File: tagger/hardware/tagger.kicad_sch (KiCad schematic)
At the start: 27 parts, among them J4 SWD, J7 TETHER_DATA, J8 DISPLAY, J9 IO_CONN, Q1 Q_NMOS_GSD, SW24 BOOT0, SW26 NRST, U2 STM32F103RGTx, Y3 CG04874-8M

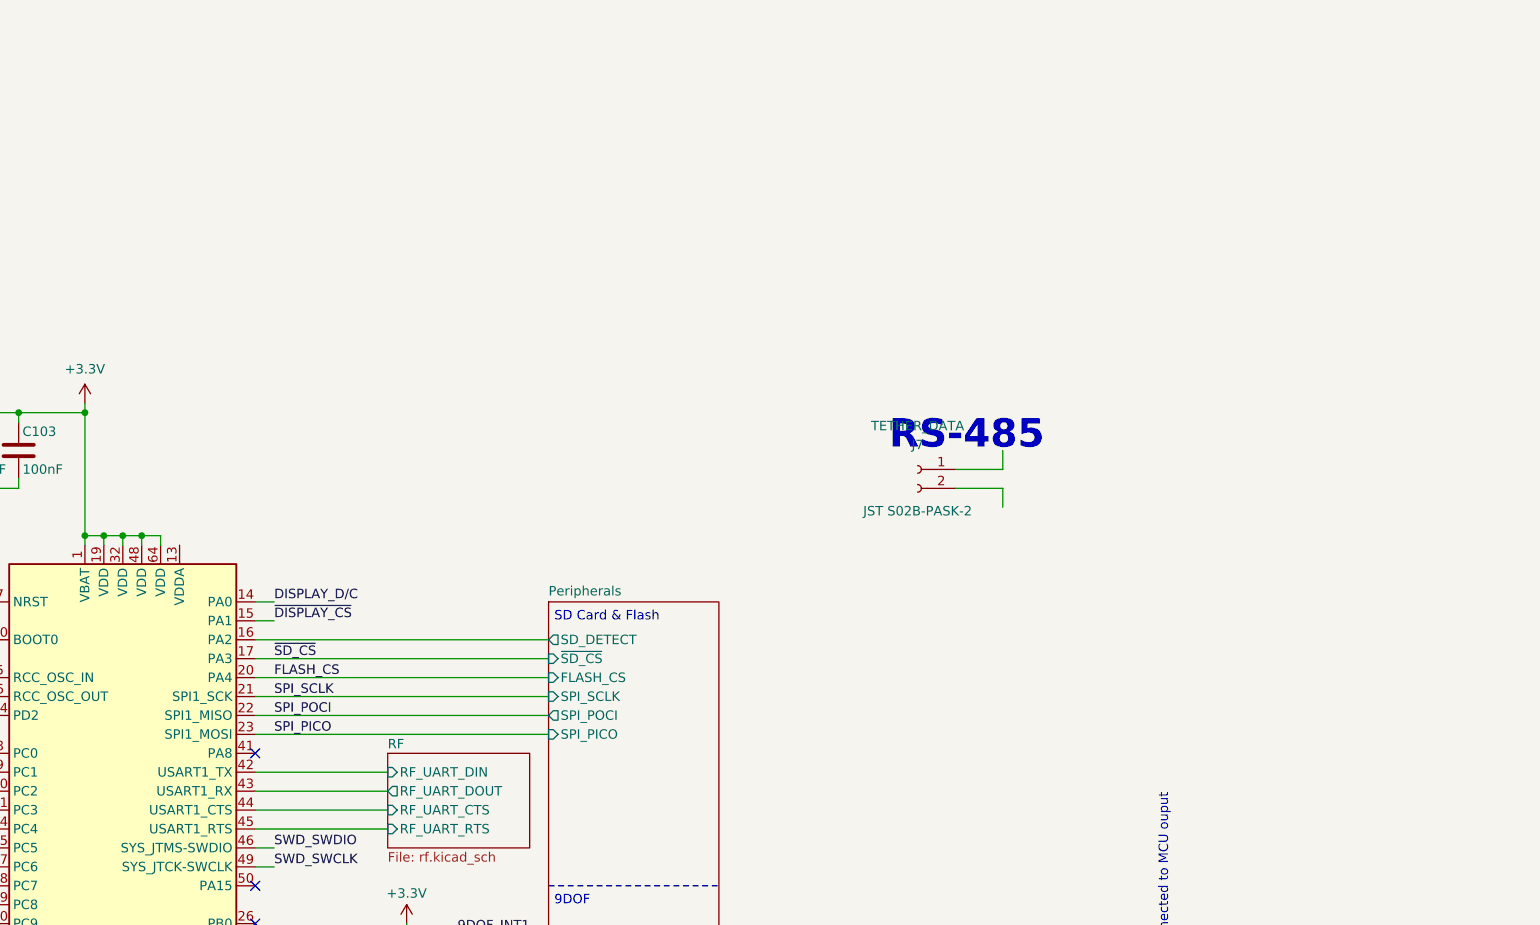
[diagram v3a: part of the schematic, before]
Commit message: feat: board routing and RS485 implementation
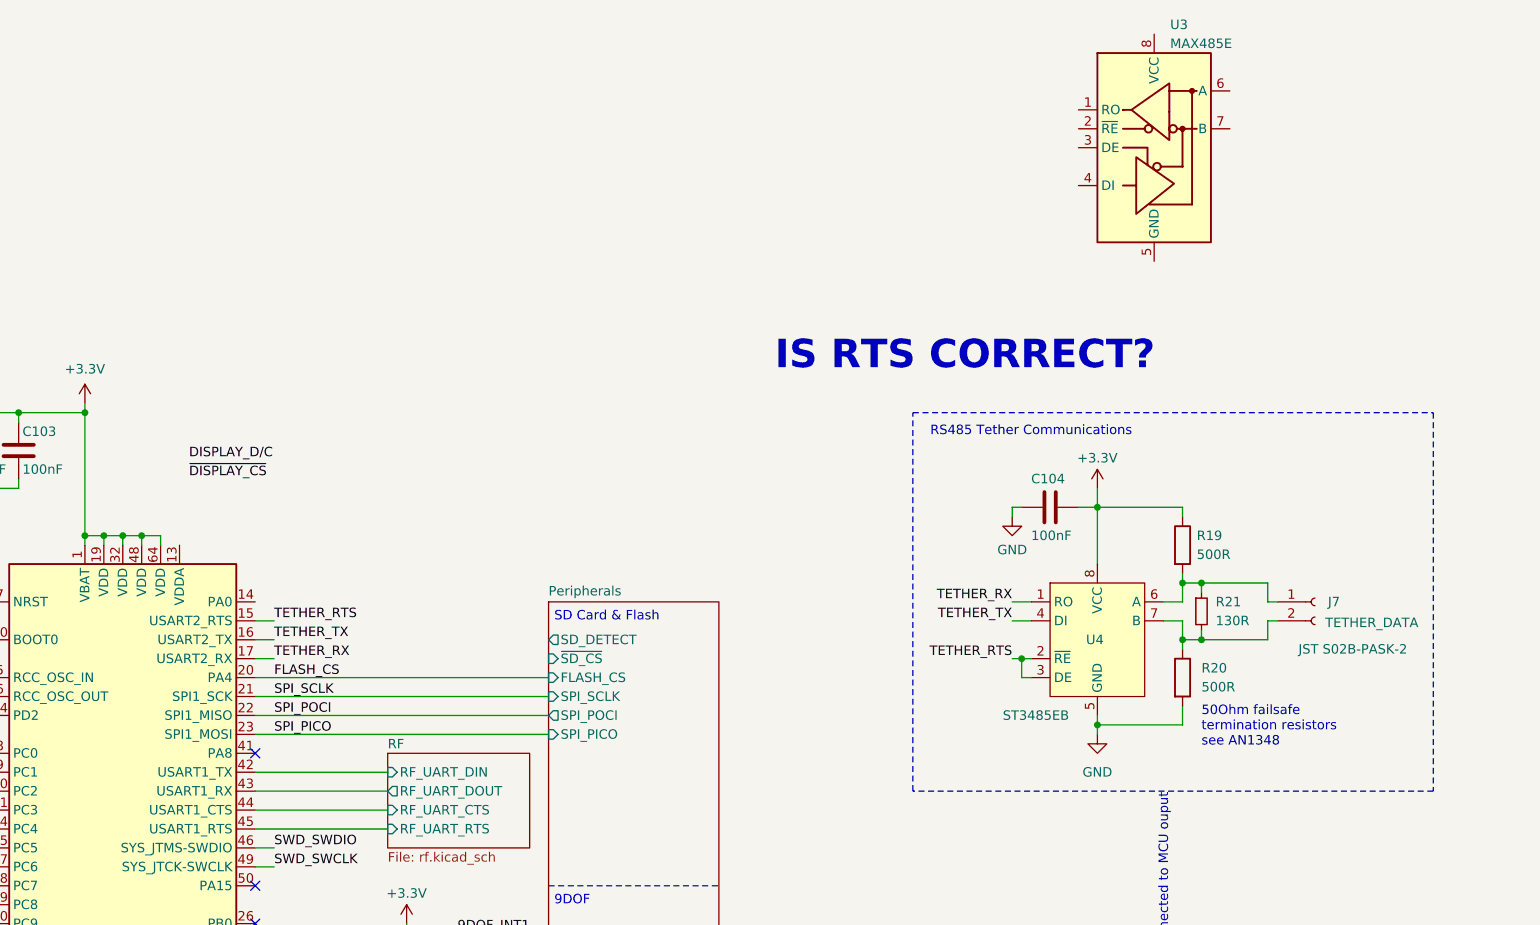
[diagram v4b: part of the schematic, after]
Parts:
- added C104: 100nF, Capacitor_SMD:C_0201_0603Metric_Pad0.64x0.40mm_HandSolder, symbol Device:C
- added R19, R20: 500R, symbol Device:R
- added R21: 130R, symbol Device:R_Small
- added U3: MAX485E, Package_SO:SOIC-8_3.9x4.9mm_P1.27mm, symbol Interface_UART:MAX485E
- added U4: ST3485EB, Package_SO:SOIC-8-N7_3.9x4.9mm_P1.27mm, symbol ST3485EBDR:ST3485EBDR
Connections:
- net +3.3V: now also C104.1, R19.1, U4.8 (VCC)
- net DISPLAY_D/C: no longer U2.14 (PA0)
- net GND: now also C104.2, R20.2, U4.5 (GND)
- net Peripherals/SD_DETECT: no longer U2.16 (PA2)
- net ~{DISPLAY_CS}: no longer U2.15 (PA1)
- net at J7.1 (Pin_1): now also R19.2, R21.1, U4.6 (A)
- net at J7.2 (Pin_2): now also R20.1, R21.2, U4.7 (B)
- net ~{SD_CS} renamed TETHER_RX
- net TETHER_RX: now also U4.1 (RO)
- new net TETHER_RTS: U2.15 (PA1), U4.2 (~{RE}), U4.3 (DE)
- new net TETHER_TX: U2.16 (PA2), U4.4 (DI)
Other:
- note added: "50Ohm failsafe termination resistors see AN1348"
- note added: "IS RTS CORRECT?"
- note added: "RS485 Tether Communications"
- note removed: "RS-485"
- moved on the sheet: J7

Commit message: feat: more board layout
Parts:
- removed R12: 0R, Resistor_SMD:R_0201_0603Metric_Pad0.64x0.40mm_HandSolder, symbol Device:R
- removed U3: MAX485E, Package_SO:SOIC-8_3.9x4.9mm_P1.27mm, symbol Interface_UART:MAX485E
- added R26: 10k, Resistor_SMD:R_0201_0603Metric_Pad0.64x0.40mm_HandSolder, symbol Device:R
- added TP1: B, TestPoint:TestPoint_Bridge_Pitch2.54mm_Drill1.0mm, symbol Connector:TestPoint
- added TP2: A, TestPoint:TestPoint_Bridge_Pitch2.54mm_Drill1.0mm, symbol Connector:TestPoint
- J7: Conn JST S02B-PASK-2 -> S02B-PASK-2
- R19, R20, R21: footprint (none) -> Resistor_SMD:R_0201_0603Metric_Pad0.64x0.40mm_HandSolder
- TP6, TP7: footprint TestPoint:TestPoint_Pad_D2.5mm -> TestPoint:TestPoint_Pad_D1.5mm
- U4: footprint Package_SO:SOIC-8-N7_3.9x4.9mm_P1.27mm -> Package_SO:SOIC-8_3.9x4.9mm_P1.27mm
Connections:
- net +3.3V: now also R26.1
- net 9DOF_INT1: now also U2.61 (PB8); no longer U2.3 (PC14)
- net 9DOF_INT2: now also U2.62 (PB9); no longer U2.4 (PC15)
- net BTN_MENU: now also U2.3 (PC14); no longer U2.53 (PC12)
- net BTN_RELOAD: now also U2.4 (PC15); no longer U2.2 (PC13)
- net BTN_TRIGGER: now also U2.2 (PC13); no longer U2.52 (PC11)
- net DISPLAY_D/C: now also U2.10 (PC2)
- net DISPLAY_RST: no longer C99.2, J4.10 (~{RESET}), SW26.2, TP6.1, U2.7 (NRST)
- net GRIP_DOUT: now also U2.9 (PC1); no longer U2.51 (PC10)
- net Peripherals/~{SD_CS}: now also U2.14 (PA0)
- net ~{DISPLAY_CS}: now also U2.41 (PA8)
- net at J7.1 (Pin_1), R19.2, R21.1: now also U4.7 (B), TP1.1; no longer U4.6 (A)
- net at J7.2 (Pin_2), R20.1, R21.2: now also U4.6 (A), TP2.1; no longer U4.7 (B)
- new net SWD_RESET: C99.2, J4.10 (~{RESET}), R26.2, SW26.2, TP6.1, U2.7 (NRST)
- no-connect marks 25 -> 14
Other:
- sheet Power ports: added none; removed 3v3_EN, 3v3_PG
- moved on the sheet: C104, J7, R19, R20, R21, U4

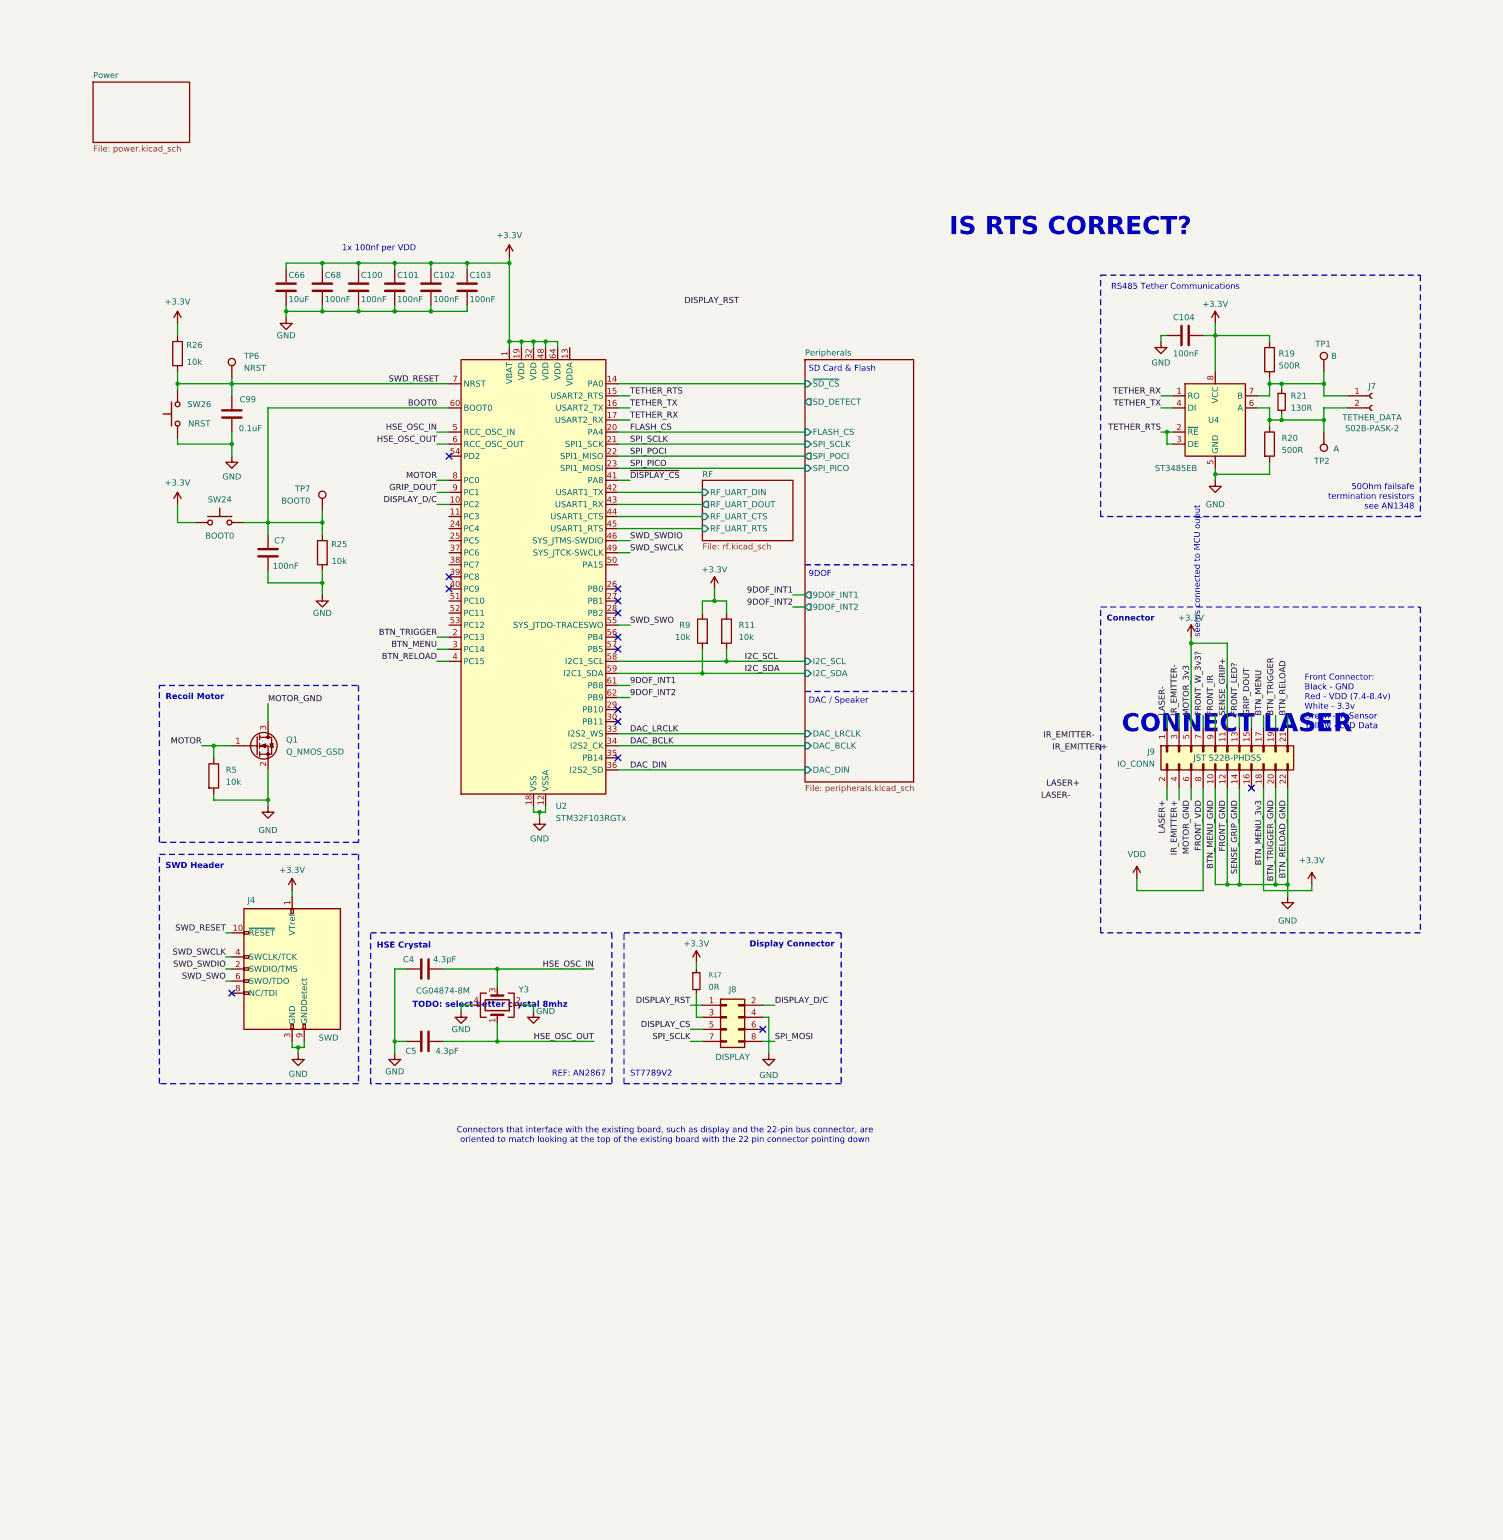
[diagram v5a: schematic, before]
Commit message: feat: various board routing changes
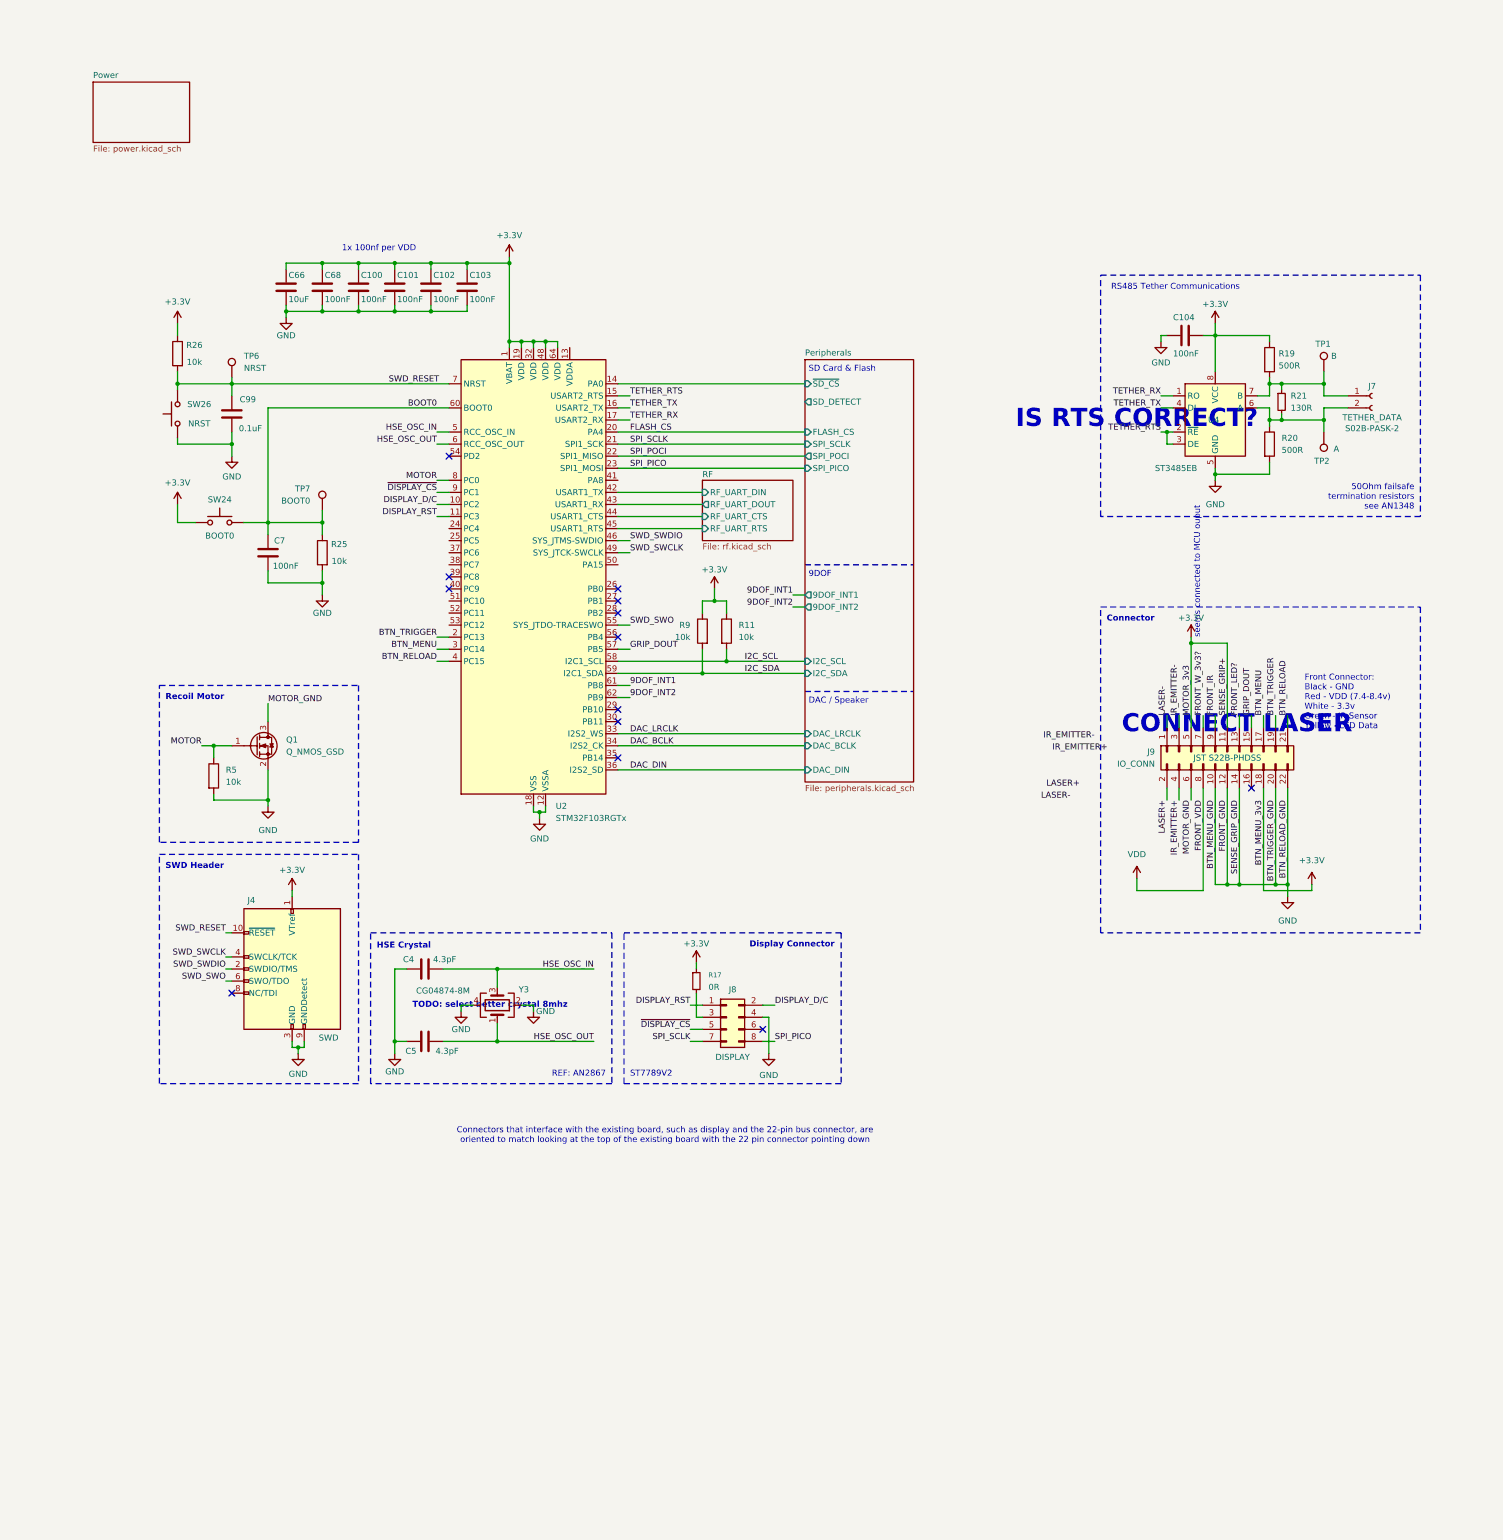
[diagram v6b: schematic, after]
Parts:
- Y3: footprint Crystal:Crystal_SMD_0603-4Pin_6.0x3.5mm -> Crystal:Crystal_SMD_Abracon_ABM3B-4Pin_5.0x3.2mm
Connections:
- net DISPLAY_CS is gone; now on net ~{DISPLAY_CS}: J8.5 (Pin_5)
- net SPI_MOSI is gone; now on net SPI_PICO: J8.8 (Pin_8)
- net DISPLAY_RST: now also U2.11 (PC3)
- net GRIP_DOUT: now also U2.57 (PB5); no longer U2.9 (PC1)
- net ~{DISPLAY_CS}: now also U2.9 (PC1); no longer U2.41 (PA8)
- no-connect marks 14 -> 13
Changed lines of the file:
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@@
 	(text "IS RTS CORRECT?"
 		(exclude_from_sim no)
-		(at 207.01 13.97 0)
+		(at 220.98 54.356 0)
 		(effects
 			(font
@@
 	)
 	(no_connect
-		(at 111.76 102.87)
-	)
-	(no_connect
 		(at 76.2 62.23)
 	)
@@
 	(wire
 		(pts
+			(xy 111.76 102.87) (xy 114.3 102.87)
+		)
+		(stroke
+			(width 0)
+			(type default)
+		)
+	)
+	(wire
+		(pts
 			(xy 248.92 52.07) (xy 246.38 52.07)
 		)
@@
 	(wire
 		(pts
-			(xy 111.76 67.31) (xy 114.3 67.31)
-		)
-		(stroke
-			(width 0)
-			(type default)
-		)
-	)
-	(wire
-		(pts
 			(xy 73.66 59.69) (xy 76.2 59.69)
 		)
@@
 	(wire
 		(pts
-			(xy 73.66 69.85) (xy 76.2 69.85)
-		)
-		(stroke
-			(width 0)
-			(type default)
-		)
-	)
-	(wire
-		(pts
 			(xy 38.1 114.3) (xy 38.1 118.11)
 		)
@@
 	(wire
 		(pts
+			(xy 73.66 69.85) (xy 76.2 69.85)
+		)
+		(stroke
+			(width 0)
+			(type default)
+		)
+	)
+	(wire
+		(pts
 			(xy 248.92 46.99) (xy 251.46 46.99)
 		)
@@
 	(wire
 		(pts
+			(xy 73.66 74.93) (xy 76.2 74.93)
+		)
+		(stroke
+			(width 0)
+			(type default)
+		)
+	)
+	(wire
+		(pts
 			(xy 226.06 36.83) (xy 226.06 38.1)
 		)
@@
 		)
 	)
-	(label "SPI_MOSI"
-		(at 144.78 185.42 0)
-		(effects
-			(font
-				(size 1.27 1.27)
-			)
-			(justify left bottom)
-		)
-	)
 	(label "MOTOR_GND"
 		(at 38.1 114.3 0)
@@
 		)
 	)
+	(label "SPI_PICO"
+		(at 144.78 185.42 0)
+		(effects
+			(font
+				(size 1.27 1.27)
+			)
+			(justify left bottom)
+		)
+	)
 	(label "SWD_RESET"
 		(at 63.5 46.99 0)
@@
 	)
 	(label "~{DISPLAY_CS}"
-		(at 114.3 67.31 0)
+		(at 73.66 69.85 180)
 		(effects
 			(font
 				(size 1.27 1.27)
 			)
-			(justify left bottom)
+			(justify right bottom)
 		)
 	)
@@
 		)
 	)
-	(label "DISPLAY_CS"
+	(label "~{DISPLAY_CS}"
 		(at 127 182.88 180)
 		(effects
@@
 	)
 	(label "GRIP_DOUT"
-		(at 73.66 69.85 180)
+		(at 114.3 102.87 0)
 		(effects
 			(font
 				(size 1.27 1.27)
 			)
-			(justify right bottom)
+			(justify left bottom)
 		)
 	)
@@
 	)
 	(label "DISPLAY_RST"
-		(at 125.73 30.48 0)
+		(at 73.66 74.93 180)
 		(effects
 			(font
 				(size 1.27 1.27)
 			)
-			(justify left bottom)
+			(justify right bottom)
 		)
 	)
@@
 			)
 		)
-		(property "Footprint" "Crystal:Crystal_SMD_0603-4Pin_6.0x3.5mm"
+		(property "Footprint" "Crystal:Crystal_SMD_Abracon_ABM3B-4Pin_5.0x3.2mm"
 			(at 86.36 177.8 0)
 			(effects
